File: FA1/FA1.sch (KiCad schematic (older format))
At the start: 18 parts, among them J1 Cin, J2 In1, J3 In2, J4 SOut, J5 COut, J6 CinThru, J7 Thru1, J8 Thru2

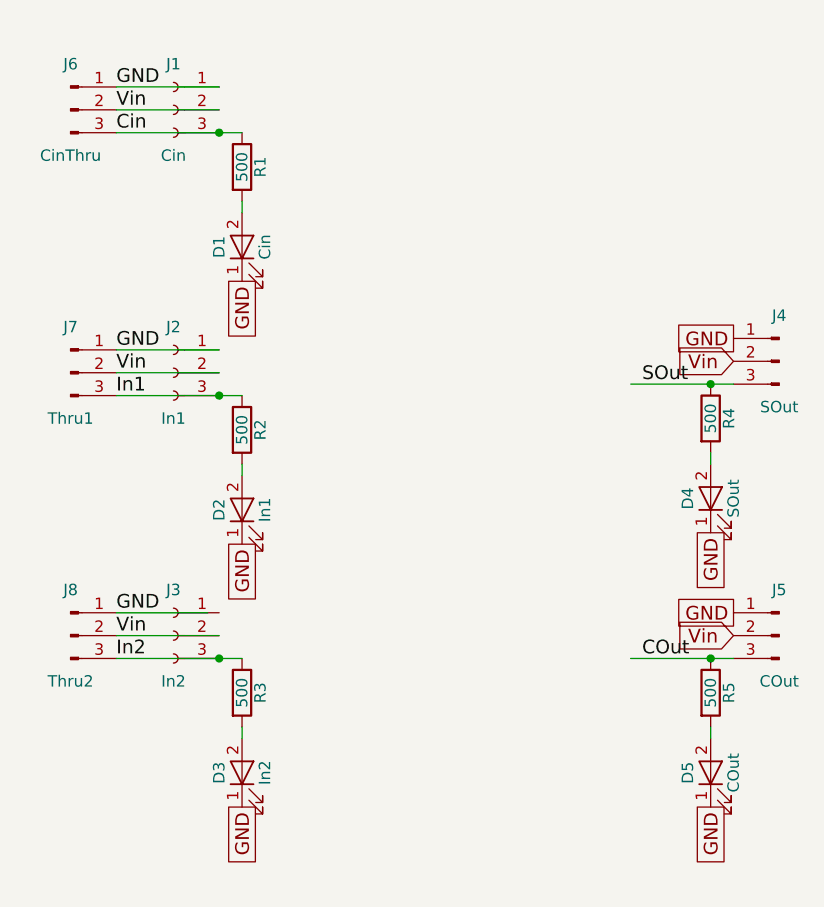
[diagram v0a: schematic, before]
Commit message: Made XOR Board and modified FA
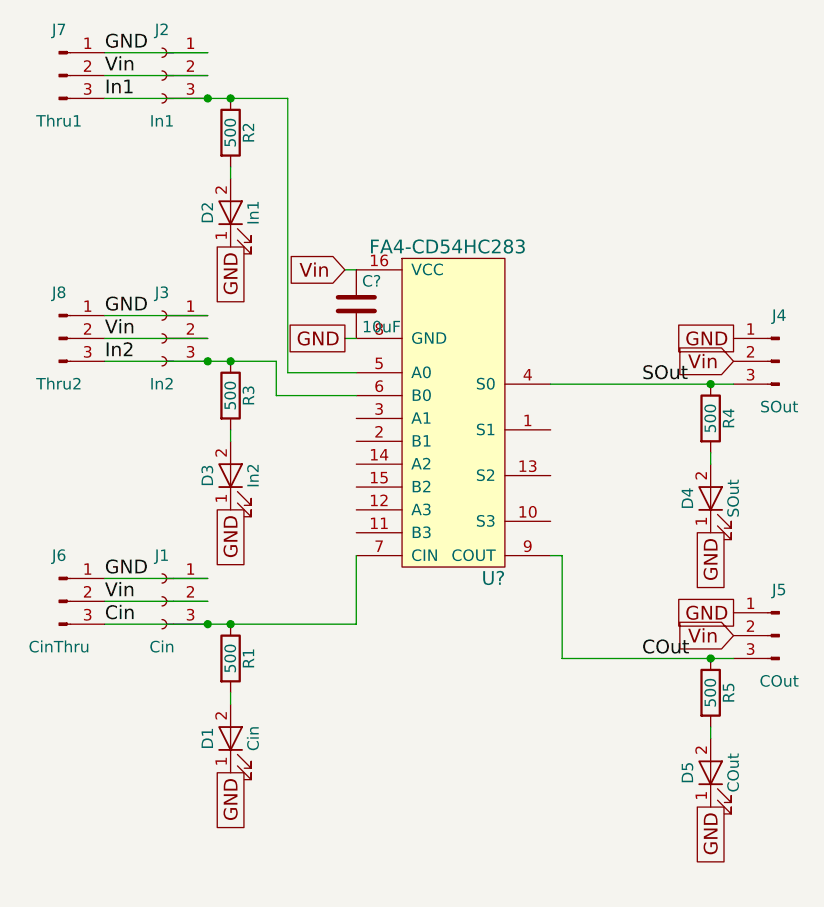
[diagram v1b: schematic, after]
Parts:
- added C?: 10uF, symbol C
- added U?: FA4-CD54HC283, symbol FA4-CD54HC283
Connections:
- wire segments 16 -> 25
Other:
- moved on the sheet: D1, D2, D3, J1, J2, J3, J6, J7, J8, R1, R2, R3
